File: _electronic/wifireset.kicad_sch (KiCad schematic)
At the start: 3 parts

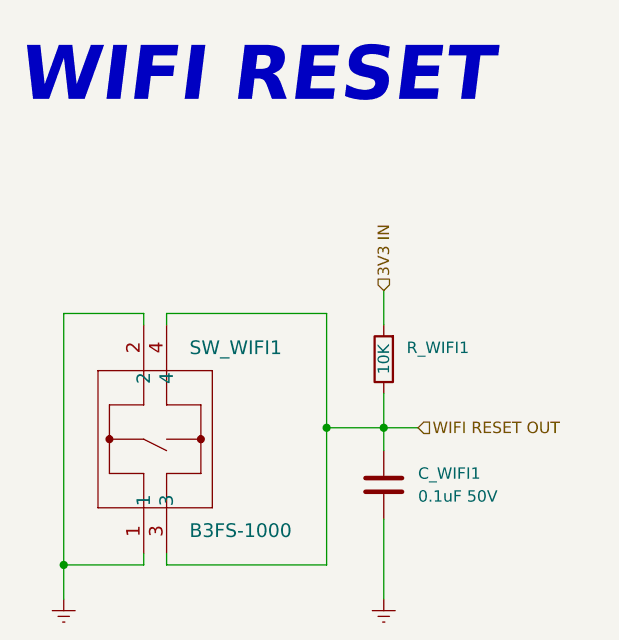
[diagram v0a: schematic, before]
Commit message: BETA first upload
nothing major done here:
* updated KiCAD files to v9
* removed alternative 6v feed-in. The proposed buck converter is fine.
* added to all components LCSC component IDs. With this, exporting the project as gerber files also automatically creates correct BOM for JLCPCB manufacturing
*
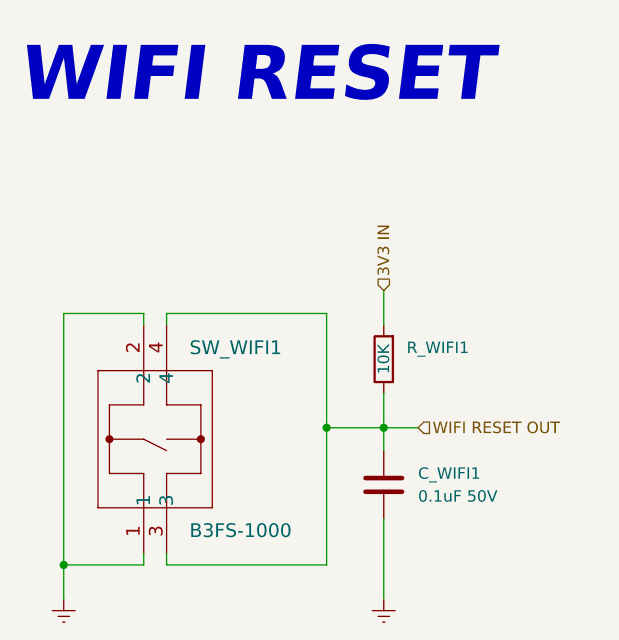
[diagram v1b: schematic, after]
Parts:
- C_WIFI1: LCSC (none) -> C14663
- R_WIFI1: LCSC (none) -> C25804
- SW_WIFI1: LCSC (none) -> C271750
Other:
- title: E-TKT v1.0 -> E-TKT v2.0 BETA

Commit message: Added CAD, cleaned up KiCAD some more
Added a FreeCAD Assembly. This will serve for minor updated to the printable parts.
Updated USB-C component to standard KiCAD libary-integrated version, because the pinout of the schematic symbol was messing with the pinout of the footprint
exported the PCB as step so it could be imported to FreeCAD
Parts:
- SW_WIFI1: footprint b3fs:B3FS-1000 -> EASYEDA2KICAD:KEY-SMD_4P-L6.0-W6.3-P4.50-LS8.0
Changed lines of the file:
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@@
 			)
 		)
-		(property "Footprint" "b3fs:B3FS-1000"
+		(property "Footprint" "EASYEDA2KICAD:KEY-SMD_4P-L6.0-W6.3-P4.50-LS8.0"
 			(at 127.254 101.6 0)
 			(effects

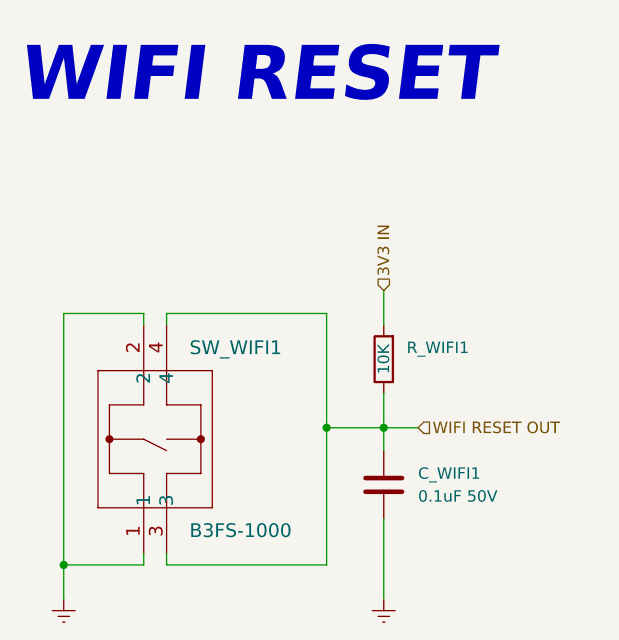
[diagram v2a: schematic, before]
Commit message: Updated layout of schematic symbol's text
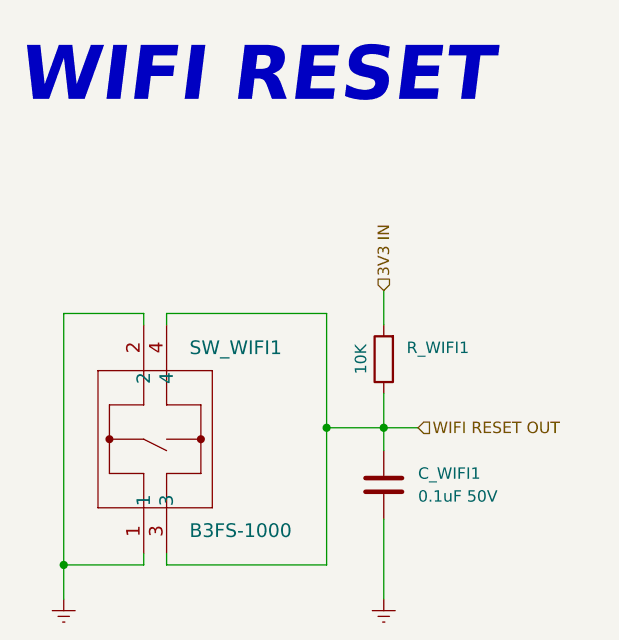
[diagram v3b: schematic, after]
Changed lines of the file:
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@@
 		)
 		(property "Value" "10K"
-			(at 160.02 92.71 90)
+			(at 157.48 92.71 90)
 			(effects
 				(font
